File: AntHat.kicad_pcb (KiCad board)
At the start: 4 copper layers, 65 x 56.5 mm, 66 parts, among them J1 Raspberry_Pi_2_3, J2 0455580003, J3 PSU Comm, J4 61900411021, J5 61900411021, J6 0353180420, J7 0353180420, Q1 DMP3013SFV-7, U1 AP64501SP-13, U2 EMC2305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

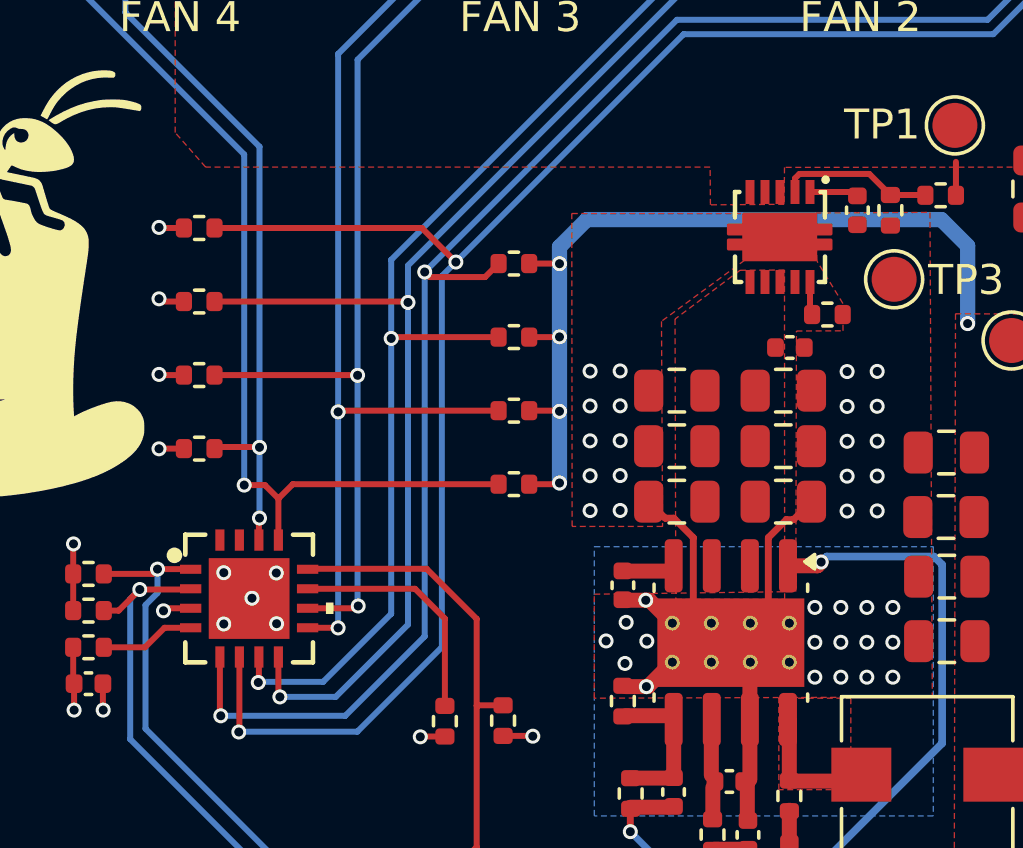
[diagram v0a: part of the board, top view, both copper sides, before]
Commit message: fixed the footprint & paste on the TPS259241 footprint. Generated and checked gerbers. Generated BOM. Generated iBOM
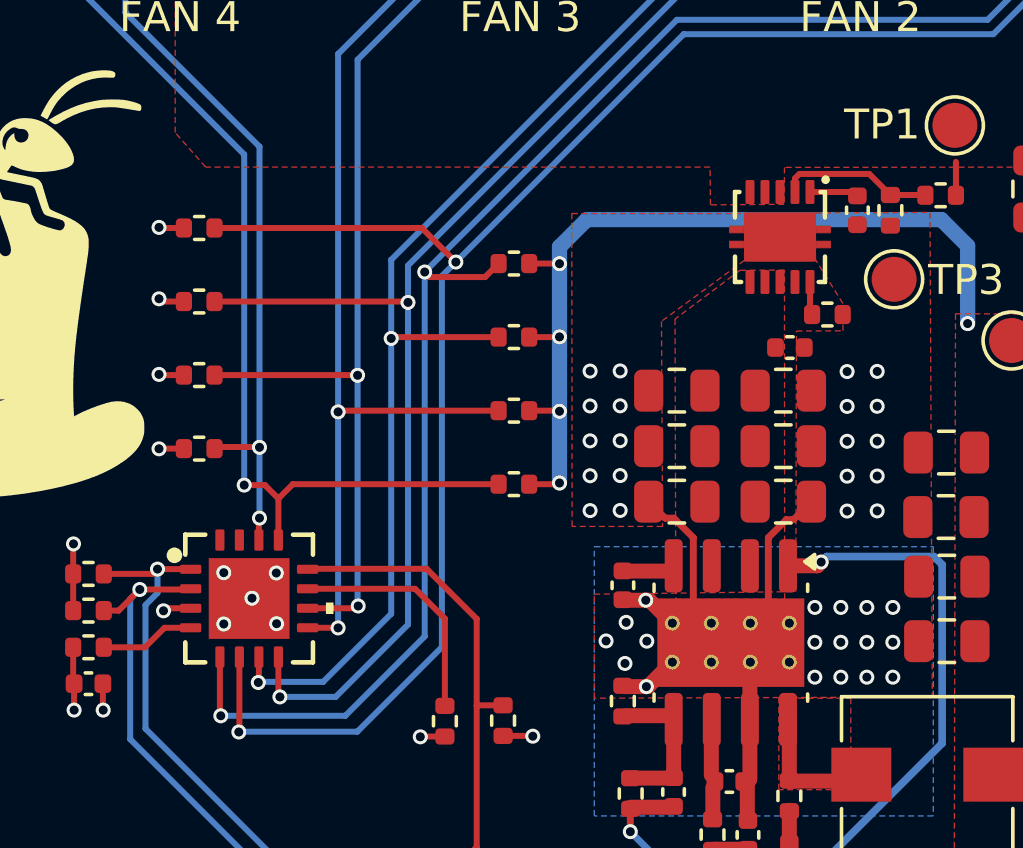
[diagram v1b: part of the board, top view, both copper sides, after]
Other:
- board text added: "FOSS || GTFO"

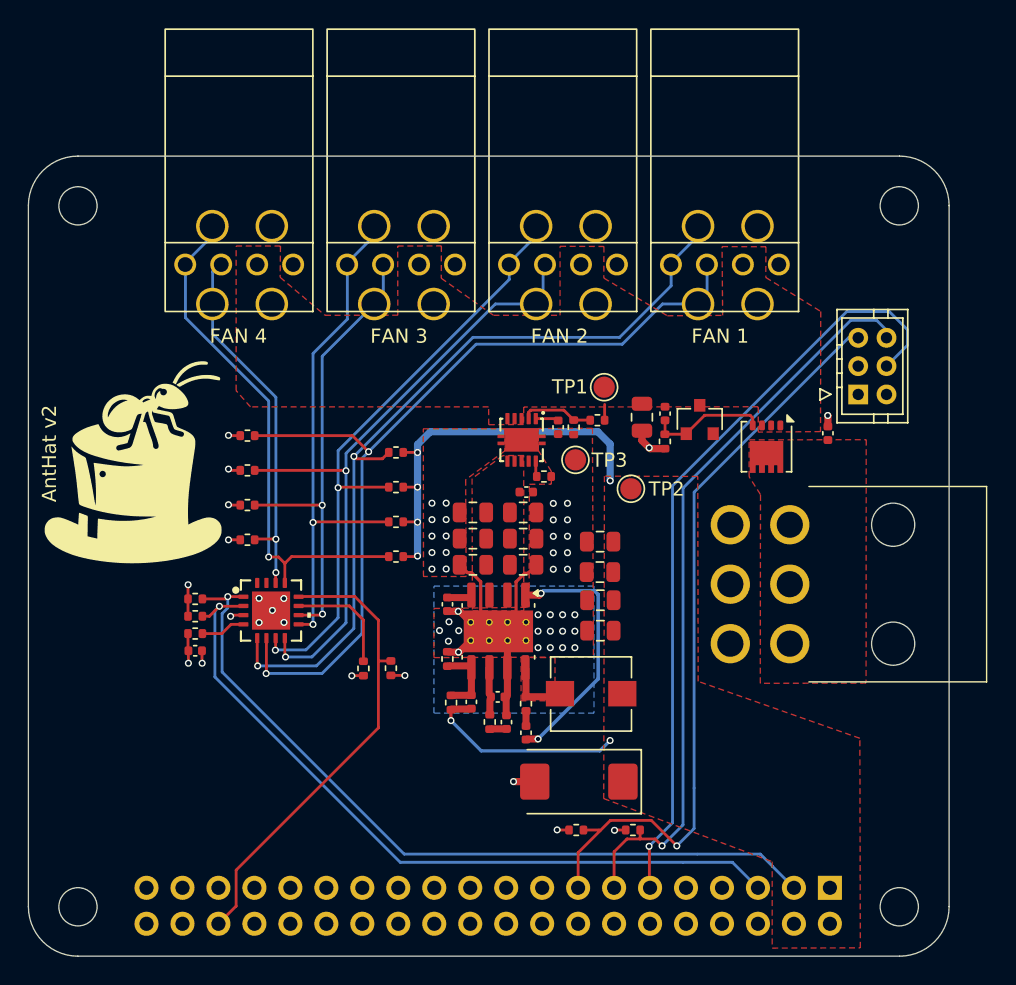
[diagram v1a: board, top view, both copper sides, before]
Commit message: added JLCPCB Parts to BOM. changed one CAP to bigger size, cleaned up layout. regenerated gerbers, BOM and CPOS
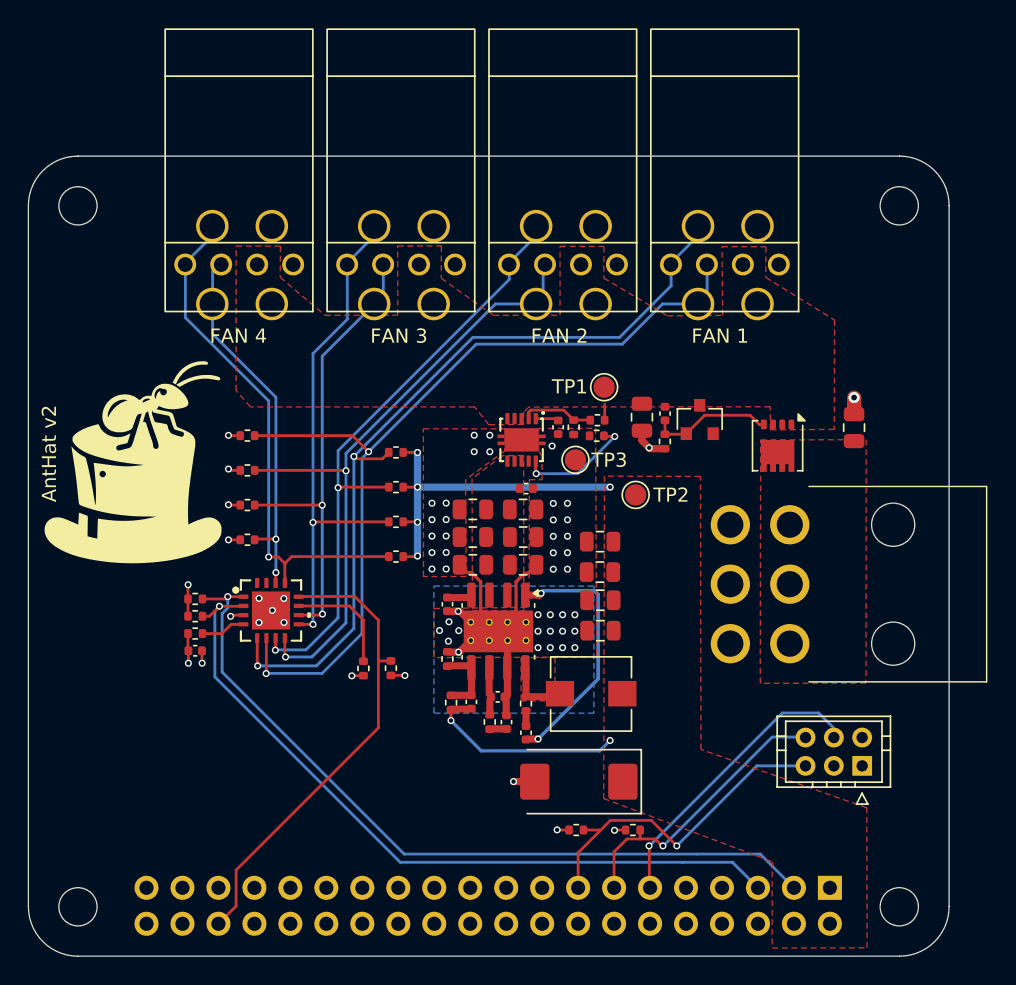
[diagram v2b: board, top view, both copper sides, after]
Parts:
- C5: value 0.1uF 100v -> 0.1uF; footprint Capacitor_SMD:C_0402_1005Metric -> Capacitor_SMD:C_0805_2012Metric
- moved J3 27.4 mm to (164.0, 111.4), turned to 0 degrees
- moved R21 4.71 mm to (147.3, 89.0), turned to 180 degrees
- moved C5 1.89 mm to (165.4, 88.5)
- moved Q1 0.79 mm to (160.1, 89.8)
- moved TP2 0.55 mm to (150.0, 93.2)
- moved C22 0.25 mm to (142.3, 92.8)
- moved C1 0.21 mm to (138.5, 94.2)
- moved C4 0.21 mm to (142.1, 94.2)
- moved C2 0.11 mm to (138.5, 96.2)
- moved C6 0.11 mm to (142.1, 96.2)
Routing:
- net /PSU_EN: track 54.5 -> 21.0 mm
- net /PSU_SCL: track 53.1 -> 20.4 mm
- net /PSU_SDA: track 53.9 -> 23.8 mm
- net Net-(U3-ILIM): track 1.11 -> 8.32 mm, vias 0 -> 2
- net /5V: track 43.4 -> 39.5 mm
- net GND: track 23.0 -> 23.4 mm, vias 47 -> 52

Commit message: switched to 6 layers. moved power vias into pads
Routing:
- net /3V3: track 12.1 -> 3.39 mm
- net GND: track 23.4 -> 19.9 mm, vias 52 -> 58
- net /5V: track 39.5 -> 36.5 mm, vias 7 -> 33
- net Net-(U3-ILIM): track 8.32 -> 7.27 mm
- net Net-(U1-SW): vias 0 -> 6
- net /VIN: vias 0 -> 8
- net /12V_LIM: vias 0 -> 24
- net /12V: vias 0 -> 11
- added copper zone on In3.Cu, net /12V
- added copper zone on In3.Cu, net /12V_LIM
- added copper zone on In3.Cu, net /5V
- added copper zone on In3.Cu, net /VIN
- added copper zone on In4.Cu, net GND
- added copper zone on In3.Cu, net Net-(U1-SW)
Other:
- copper layers 4 -> 6
- board text added: "AntHat v3"
- board text removed: "AntHat v2"

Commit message: added OSHWA logo. removed old gerbers
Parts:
- added G2: OSHWA-LOGO, AntHat:oshwa_logo, F.Cu at (114.7, 111.6)

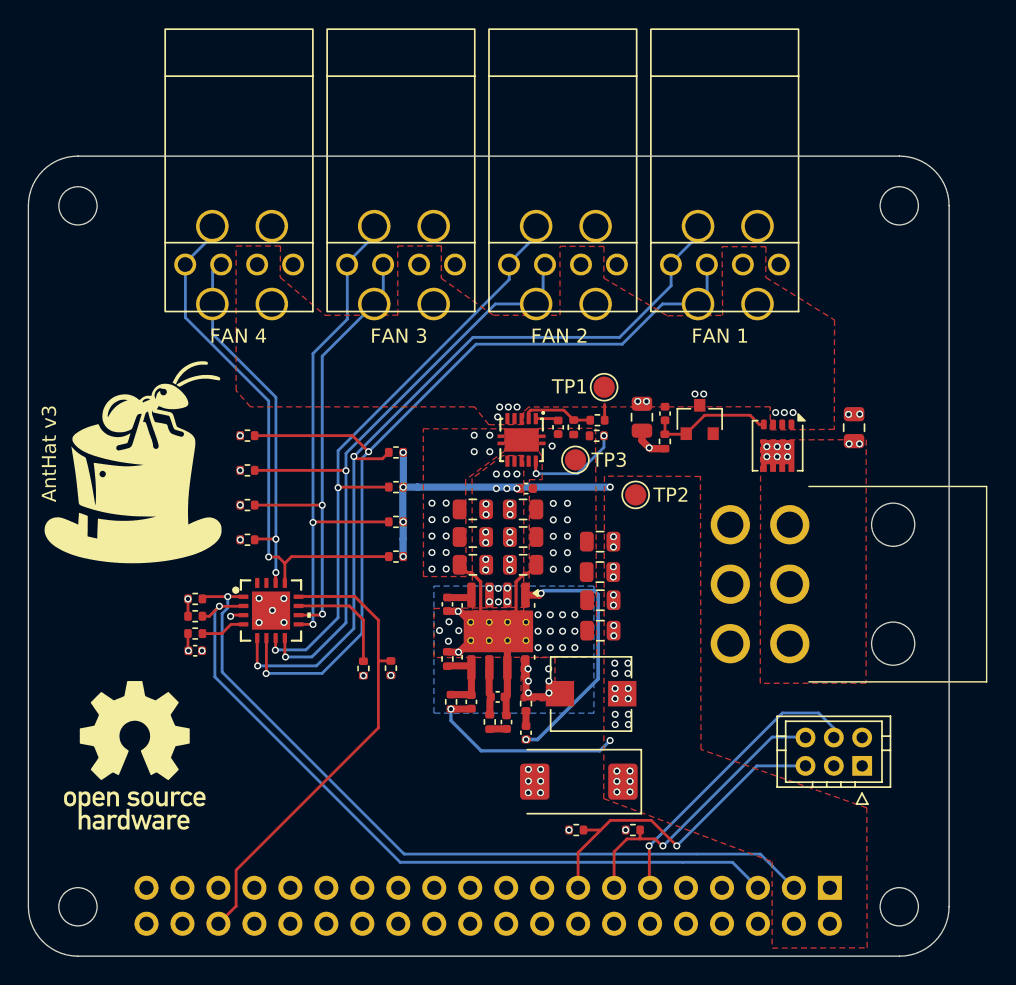
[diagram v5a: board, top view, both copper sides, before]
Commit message: added fiducials
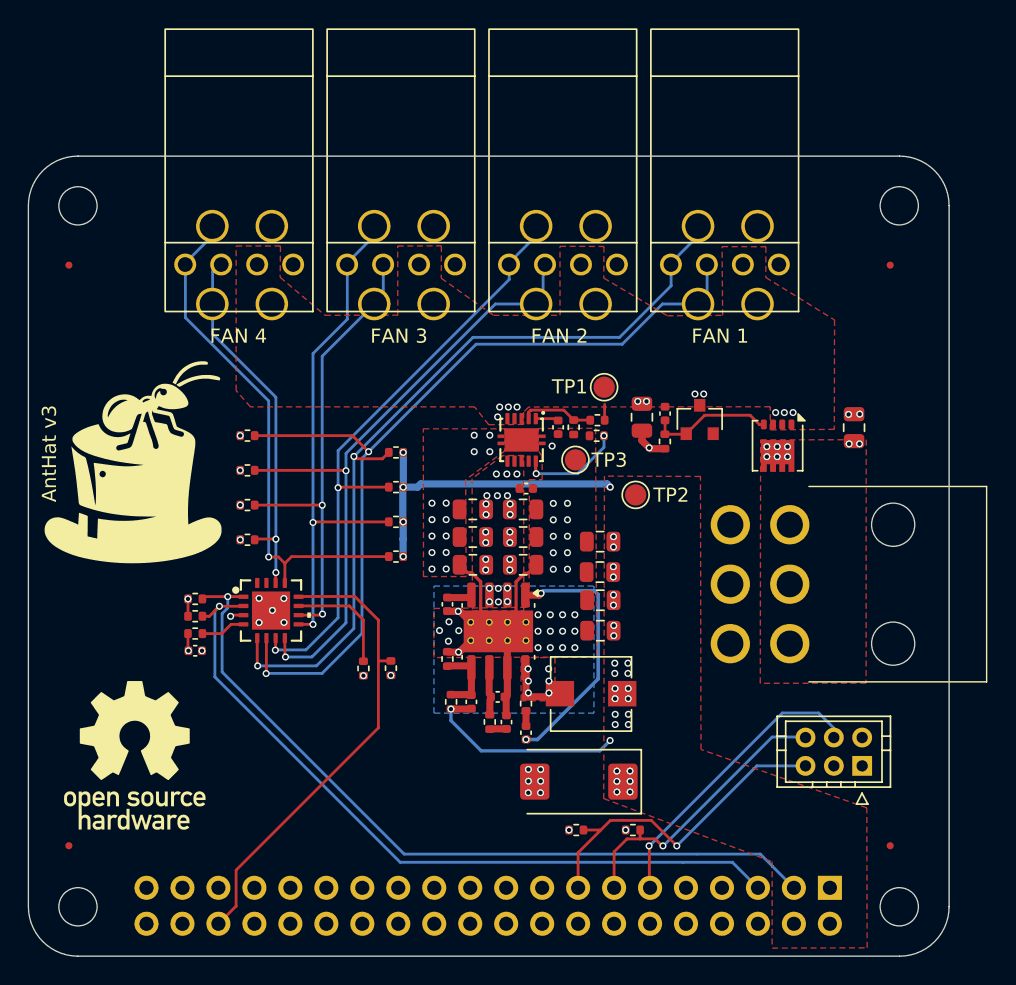
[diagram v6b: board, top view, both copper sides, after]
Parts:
- added FID1: Fiducial, Fiducial:Fiducial_0.5mm_Mask1mm, F.Cu at (110.0, 77.0)
- added FID2: Fiducial, Fiducial:Fiducial_0.5mm_Mask1mm, F.Cu at (168.0, 77.0)
- added FID3: Fiducial, Fiducial:Fiducial_0.5mm_Mask1mm, F.Cu at (168.0, 118.0)
- added FID4: Fiducial, Fiducial:Fiducial_0.5mm_Mask1mm, F.Cu at (110.0, 118.0)
